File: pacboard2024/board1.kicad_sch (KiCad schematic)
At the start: 18 parts, among them J1 Conn_01x05_Female, J6 XT30 Male Connector, U1 BNO085, U2 ProS3

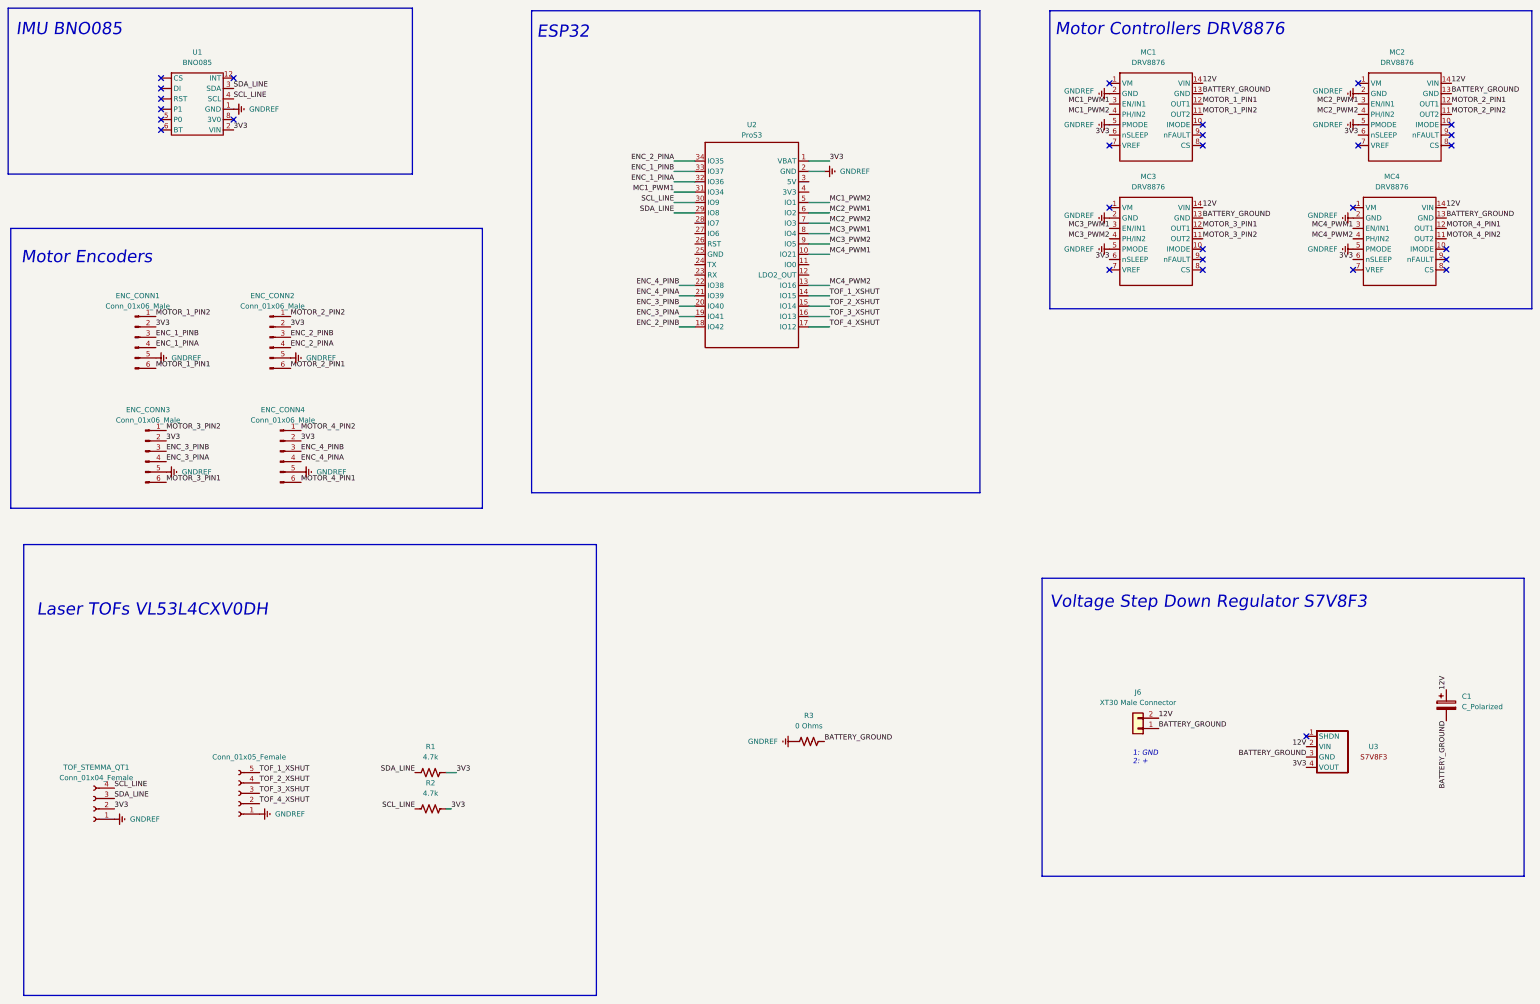
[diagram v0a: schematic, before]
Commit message: schematic done(?) and layout
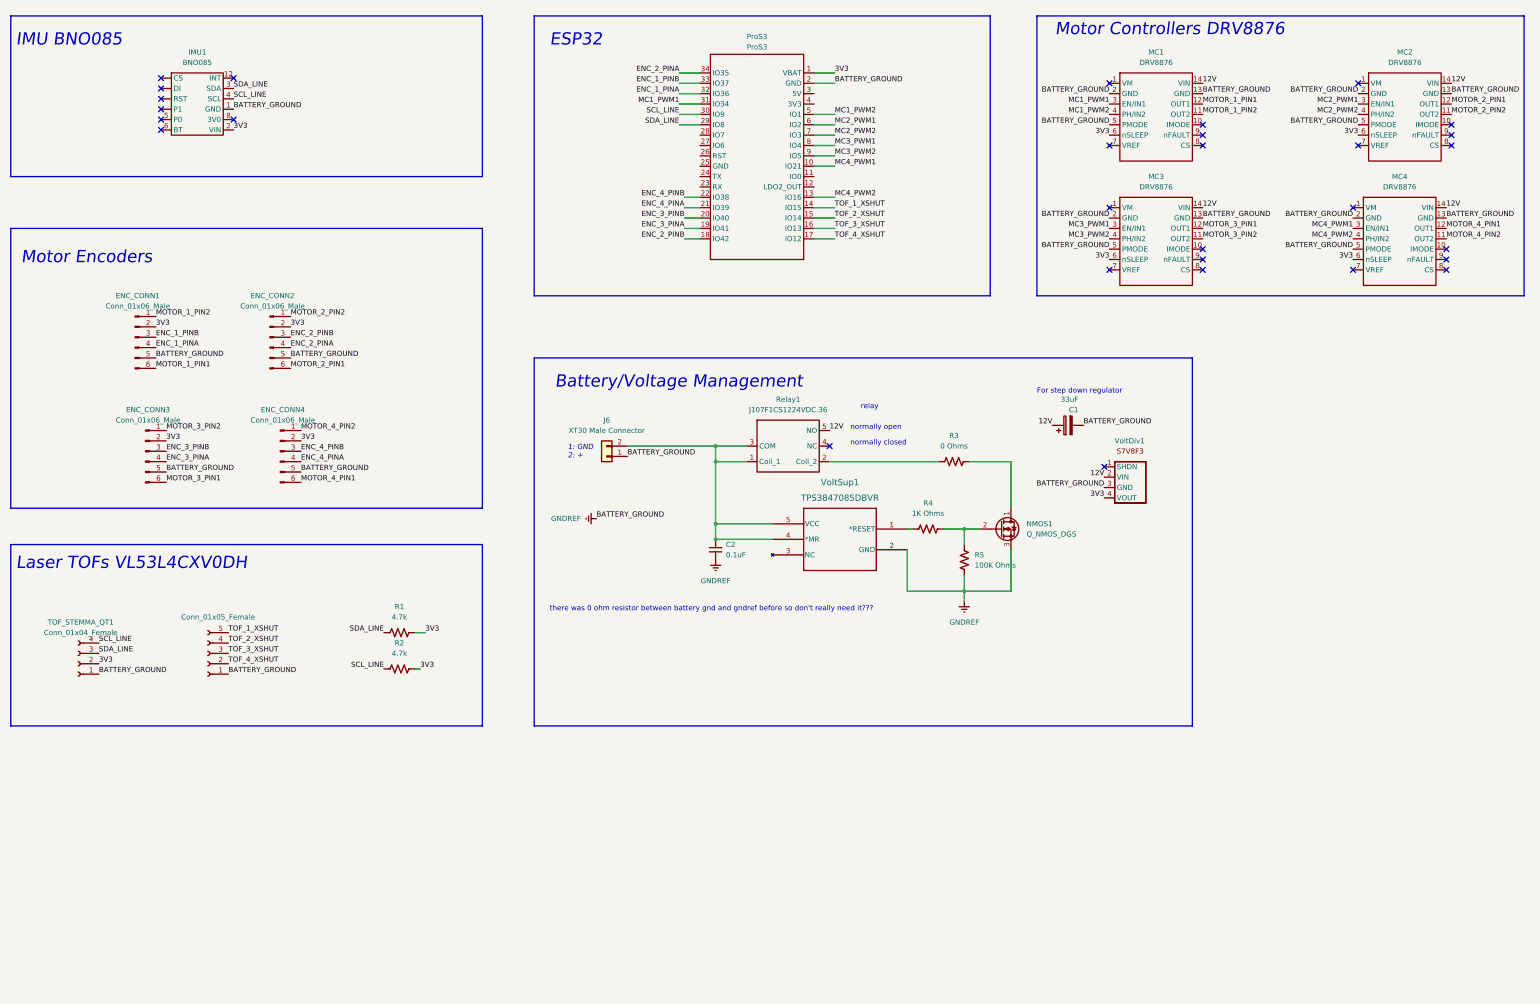
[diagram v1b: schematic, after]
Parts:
- added C2: 0.1uF, Capacitor_SMD:C_0805_2012Metric_Pad1.18x1.45mm_HandSolder, symbol Device:C_Small
- added NMOS1: Q_NMOS_DGS, Package_TO_SOT_SMD:SOT-23, symbol Device:Q_NMOS_DGS
- added R4: 1K Ohms, Resistor_SMD:R_0805_2012Metric, symbol Device:R_US
- added R5: 100K Ohms, Resistor_SMD:R_0805_2012Metric, symbol Device:R_US
- added Relay1: J107F1CS1224VDC.36, board1_footprints:J107, symbol board1_libs:J107F1CS1224VDC.36
- added VoltSup1: TPS3847085DBVR, DBV5_TEX, symbol board1_libs:TPS3847085DBVR
- C1: value C_Polarized -> 33uF
- renumbered U1 to IMU1, U2 to ProS3, U3 to VoltDiv1
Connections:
- net 12V: now also Relay1.5 (NO); no longer J6.2 (Pin_2)
- net GNDREF: now also C1.2, J6.1 (Pin_1), MC1.13 (GND), MC2.13 (GND), MC3.13 (GND), MC4.13 (GND), VoltDiv1.3 (GND), C2.2, NMOS1.3 (S), R5.1, VoltSup1.2 (GND); no longer R3.1
- removed net BATTERY_GROUND: C1.2, J6.1 (Pin_1), MC1.13 (GND), MC2.13 (GND), MC3.13 (GND), MC4.13 (GND), R3.2, VoltDiv1.3 (GND)
- new net: C2.1, J6.2 (Pin_2), Relay1.1 (Coil_1), Relay1.3 (COM), VoltSup1.4 (*MR), VoltSup1.5 (VCC)
- new net: R3.2, Relay1.2 (Coil_2)
- new net: NMOS1.1 (D), R3.1
- new net: R4.1, VoltSup1.1 (*RESET)
- new net: NMOS1.2 (G), R4.2, R5.2
- no-connect marks 29 -> 30
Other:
- note added: "Battery/Voltage Management"
- note added: "For step down regulator"
- note added: "normally closed"
- note added: "normally open"
- note added: "relay"
- note added: "there was 0 ohm resistor between battery gnd and gndref before so don't really need it???"
- note removed: "Voltage Step Down Regulator S7V8F3"
- moved on the sheet: C1, J6, ProS3, R1, R2, TOF_STEMMA_QT1, VoltDiv1

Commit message: routing to pcb
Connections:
- net ENC_1_PINA: now also ProS3.17 (IO12); no longer ProS3.32 (IO36)
- net ENC_1_PINB: now also ProS3.18 (IO42); no longer ProS3.33 (IO37)
- net ENC_2_PINA: now also ProS3.20 (IO40); no longer ProS3.34 (IO35)
- net ENC_2_PINB: now also ProS3.19 (IO41); no longer ProS3.18 (IO42)
- net ENC_3_PINA: now also ProS3.32 (IO36); no longer ProS3.19 (IO41)
- net ENC_3_PINB: now also ProS3.31 (IO34); no longer ProS3.20 (IO40)
- net ENC_4_PINA: now also ProS3.16 (IO13); no longer ProS3.21 (IO39)
- net ENC_4_PINB: now also ProS3.15 (IO14); no longer ProS3.22 (IO38)
- net MC1_PWM1: now also ProS3.14 (IO15); no longer ProS3.31 (IO34)
- net MC1_PWM2: now also ProS3.13 (IO16); no longer ProS3.5 (IO1)
- net MC2_PWM1: now also ProS3.21 (IO39); no longer ProS3.6 (IO2)
- net MC2_PWM2: now also ProS3.22 (IO38); no longer ProS3.7 (IO3)
- net MC3_PWM1: now also ProS3.33 (IO37); no longer ProS3.8 (IO4)
- net MC3_PWM2: now also ProS3.34 (IO35); no longer ProS3.9 (IO5)
- net MC4_PWM1: now also ProS3.9 (IO5); no longer ProS3.10 (IO21)
- net MC4_PWM2: now also ProS3.10 (IO21); no longer ProS3.13 (IO16)
- net TOF_1_XSHUT: now also ProS3.5 (IO1); no longer ProS3.14 (IO15)
- net TOF_2_XSHUT: now also ProS3.6 (IO2); no longer ProS3.15 (IO14)
- net TOF_3_XSHUT: now also ProS3.7 (IO3); no longer ProS3.16 (IO13)
- net TOF_4_XSHUT: now also ProS3.8 (IO4); no longer ProS3.17 (IO12)
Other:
- note added: "2: + 1: GND"
- note removed: "1: GND 2: +"
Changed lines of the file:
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@@
     (effects (font (size 3 3) italic) (justify left bottom))
   )
-  (text "1: GND\n2: +" (at 160.655 130.175 0)
+  (text "2: +\n1: GND" (at 160.655 130.175 0)
     (effects (font (size 1.27 1.27) italic) (justify left bottom))
   )
@@
     (effects (font (size 1.27 1.27)) (justify left bottom))
   )
-  (label "MC3_PWM2" (at 226.06 55.88 0) (fields_autoplaced)
-    (effects (font (size 1.27 1.27)) (justify left bottom))
+  (label "MC3_PWM2" (at 187.96 35.56 180) (fields_autoplaced)
+    (effects (font (size 1.27 1.27)) (justify right bottom))
   )
   (label "BATTERY_GROUND" (at 353.06 78.74 180) (fields_autoplaced)
@@
     (effects (font (size 1.27 1.27)) (justify left bottom))
   )
-  (label "MC4_PWM1" (at 226.06 58.42 0) (fields_autoplaced)
+  (label "MC4_PWM1" (at 226.06 55.88 0) (fields_autoplaced)
     (effects (font (size 1.27 1.27)) (justify left bottom))
   )
@@
     (effects (font (size 1.27 1.27)) (justify left bottom))
   )
-  (label "TOF_2_XSHUT" (at 226.06 71.12 0) (fields_autoplaced)
+  (label "TOF_2_XSHUT" (at 226.06 48.26 0) (fields_autoplaced)
     (effects (font (size 1.27 1.27)) (justify left bottom))
   )
@@
     (effects (font (size 1.27 1.27)) (justify left bottom))
   )
-  (label "ENC_4_PINB" (at 189.23 66.04 180) (fields_autoplaced)
-    (effects (font (size 1.27 1.27)) (justify right bottom))
-  )
-  (label "ENC_3_PINA" (at 189.23 73.66 180) (fields_autoplaced)
+  (label "ENC_4_PINB" (at 226.06 71.12 0) (fields_autoplaced)
+    (effects (font (size 1.27 1.27)) (justify left bottom))
+  )
+  (label "ENC_3_PINA" (at 187.96 40.64 180) (fields_autoplaced)
     (effects (font (size 1.27 1.27)) (justify right bottom))
   )
@@
     (effects (font (size 1.27 1.27)) (justify left bottom))
   )
-  (label "MC1_PWM2" (at 226.06 45.72 0) (fields_autoplaced)
+  (label "MC1_PWM2" (at 226.06 66.04 0) (fields_autoplaced)
     (effects (font (size 1.27 1.27)) (justify left bottom))
   )
@@
     (effects (font (size 1.27 1.27)) (justify left bottom))
   )
-  (label "TOF_3_XSHUT" (at 226.06 73.66 0) (fields_autoplaced)
+  (label "TOF_3_XSHUT" (at 226.06 50.8 0) (fields_autoplaced)
     (effects (font (size 1.27 1.27)) (justify left bottom))
   )
@@
     (effects (font (size 1.27 1.27)) (justify left bottom))
   )
-  (label "MC1_PWM1" (at 187.96 43.18 180) (fields_autoplaced)
-    (effects (font (size 1.27 1.27)) (justify right bottom))
+  (label "MC1_PWM1" (at 226.06 68.58 0) (fields_autoplaced)
+    (effects (font (size 1.27 1.27)) (justify left bottom))
   )
   (label "BATTERY_GROUND" (at 292.1 137.16 180) (fields_autoplaced)
     (effects (font (size 1.27 1.27)) (justify right bottom))
   )
-  (label "TOF_4_XSHUT" (at 226.06 76.2 0) (fields_autoplaced)
+  (label "TOF_4_XSHUT" (at 226.06 53.34 0) (fields_autoplaced)
     (effects (font (size 1.27 1.27)) (justify left bottom))
   )
@@
     (effects (font (size 1.27 1.27)) (justify left bottom))
   )
-  (label "ENC_3_PINB" (at 189.23 71.12 180) (fields_autoplaced)
-    (effects (font (size 1.27 1.27)) (justify right bottom))
-  )
-  (label "ENC_1_PINA" (at 187.96 40.64 180) (fields_autoplaced)
-    (effects (font (size 1.27 1.27)) (justify right bottom))
+  (label "ENC_3_PINB" (at 187.96 43.18 180) (fields_autoplaced)
+    (effects (font (size 1.27 1.27)) (justify right bottom))
+  )
+  (label "ENC_1_PINA" (at 226.06 76.2 0) (fields_autoplaced)
+    (effects (font (size 1.27 1.27)) (justify left bottom))
   )
   (label "BATTERY_GROUND" (at 62.23 133.35 0) (fields_autoplaced)
@@
     (effects (font (size 1.27 1.27)) (justify right bottom))
   )
-  (label "TOF_1_XSHUT" (at 226.06 68.58 0) (fields_autoplaced)
+  (label "TOF_1_XSHUT" (at 226.06 45.72 0) (fields_autoplaced)
     (effects (font (size 1.27 1.27)) (justify left bottom))
   )
@@
     (effects (font (size 1.27 1.27)) (justify left bottom))
   )
-  (label "MC3_PWM1" (at 226.06 53.34 0) (fields_autoplaced)
-    (effects (font (size 1.27 1.27)) (justify left bottom))
+  (label "MC3_PWM1" (at 187.96 38.1 180) (fields_autoplaced)
+    (effects (font (size 1.27 1.27)) (justify right bottom))
   )
   (label "3V3" (at 293.37 81.28 180) (fields_autoplaced)
@@
     (effects (font (size 1.27 1.27)) (justify left bottom))
   )
-  (label "ENC_1_PINB" (at 187.96 38.1 180) (fields_autoplaced)
+  (label "ENC_1_PINB" (at 189.23 76.2 180) (fields_autoplaced)
     (effects (font (size 1.27 1.27)) (justify right bottom))
   )
@@
     (effects (font (size 1.27 1.27)) (justify right bottom))
   )
-  (label "ENC_4_PINA" (at 189.23 68.58 180) (fields_autoplaced)
-    (effects (font (size 1.27 1.27)) (justify right bottom))
+  (label "ENC_4_PINA" (at 226.06 73.66 0) (fields_autoplaced)
+    (effects (font (size 1.27 1.27)) (justify left bottom))
   )
   (label "MC2_PWM2" (at 354.33 45.72 180) (fields_autoplaced)
@@
     (effects (font (size 1.27 1.27)) (justify right bottom))
   )
-  (label "ENC_2_PINB" (at 189.23 76.2 180) (fields_autoplaced)
+  (label "ENC_2_PINB" (at 189.23 73.66 180) (fields_autoplaced)
     (effects (font (size 1.27 1.27)) (justify right bottom))
   )
@@
     (effects (font (size 1.27 1.27)) (justify left bottom))
   )
-  (label "MC2_PWM1" (at 226.06 48.26 0) (fields_autoplaced)
-    (effects (font (size 1.27 1.27)) (justify left bottom))
+  (label "MC2_PWM1" (at 189.23 68.58 180) (fields_autoplaced)
+    (effects (font (size 1.27 1.27)) (justify right bottom))
   )
   (label "3V3" (at 125.73 172.72 0) (fields_autoplaced)
@@
     (effects (font (size 1.27 1.27)) (justify left bottom))
   )
-  (label "ENC_2_PINA" (at 187.96 35.56 180) (fields_autoplaced)
+  (label "ENC_2_PINA" (at 189.23 71.12 180) (fields_autoplaced)
     (effects (font (size 1.27 1.27)) (justify right bottom))
   )
@@
     (effects (font (size 1.27 1.27)) (justify right bottom))
   )
-  (label "MC4_PWM2" (at 226.06 66.04 0) (fields_autoplaced)
+  (label "MC4_PWM2" (at 226.06 58.42 0) (fields_autoplaced)
     (effects (font (size 1.27 1.27)) (justify left bottom))
   )
@@
     (effects (font (size 1.27 1.27)) (justify right bottom))
   )
-  (label "MC2_PWM2" (at 226.06 50.8 0) (fields_autoplaced)
-    (effects (font (size 1.27 1.27)) (justify left bottom))
+  (label "MC2_PWM2" (at 189.23 66.04 180) (fields_autoplaced)
+    (effects (font (size 1.27 1.27)) (justify right bottom))
   )
   (label "3V3" (at 59.69 97.79 0) (fields_autoplaced)
